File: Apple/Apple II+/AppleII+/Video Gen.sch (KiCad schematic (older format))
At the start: 46 parts, among them J14B Aux Video, K14 VIDEO OUT, Q3 2N3904, Q6 2N3904

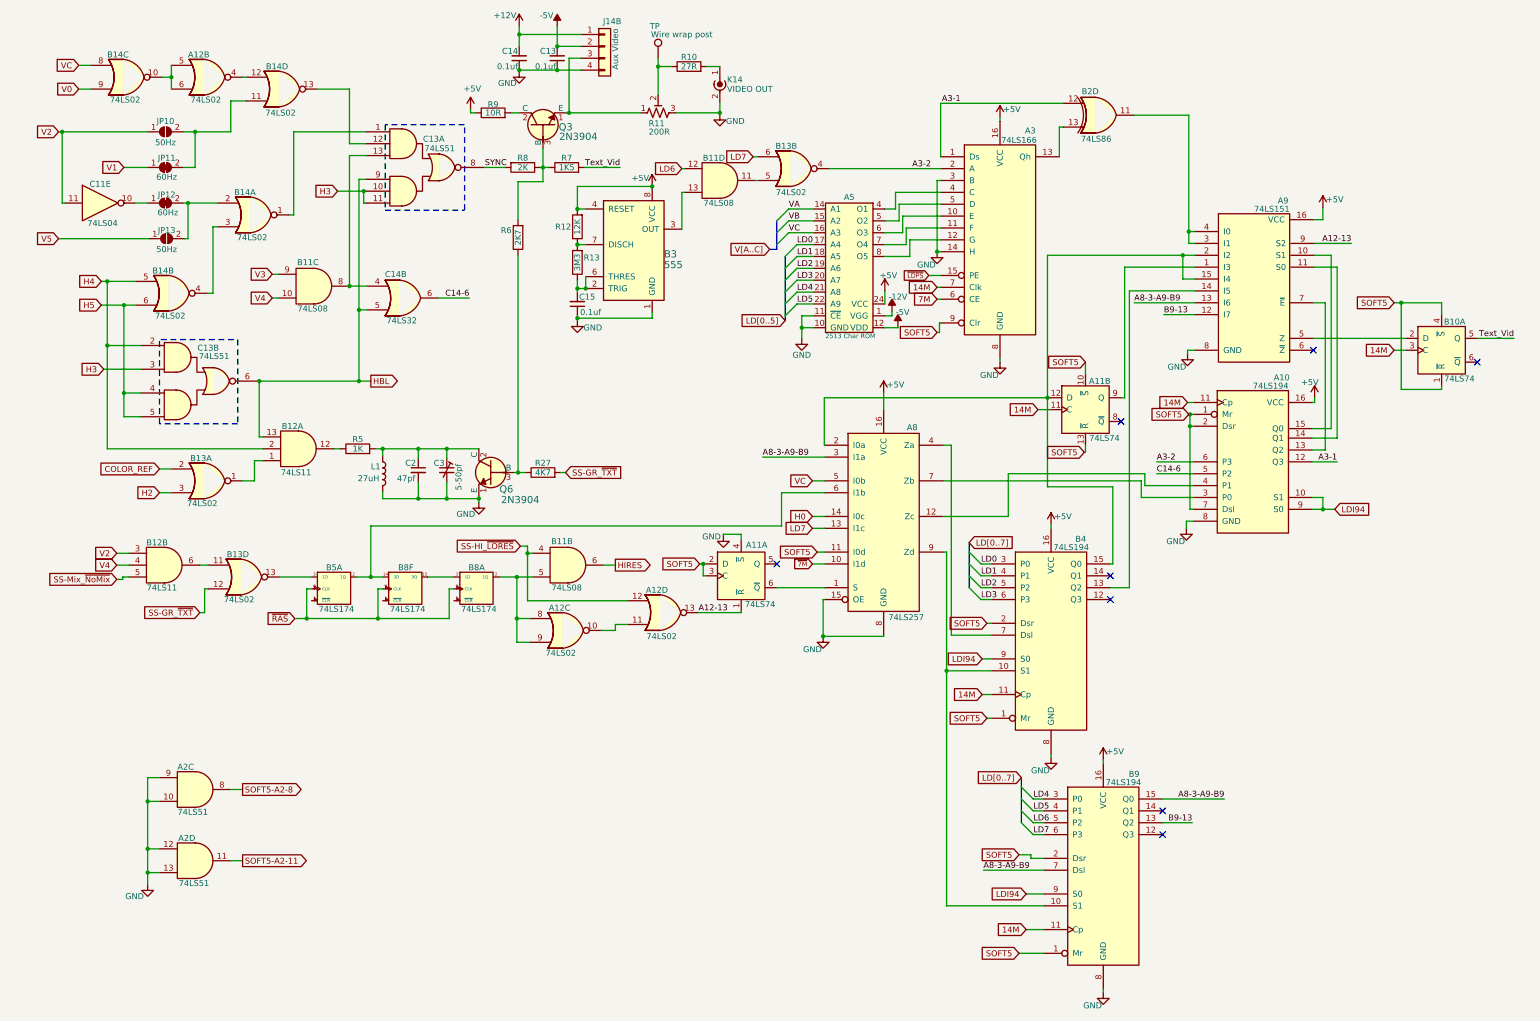
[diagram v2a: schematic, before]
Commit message: Created DiskII project folder and moved DiskII sheet to it, also fixed some signal designations, created sheet for peripheral slots
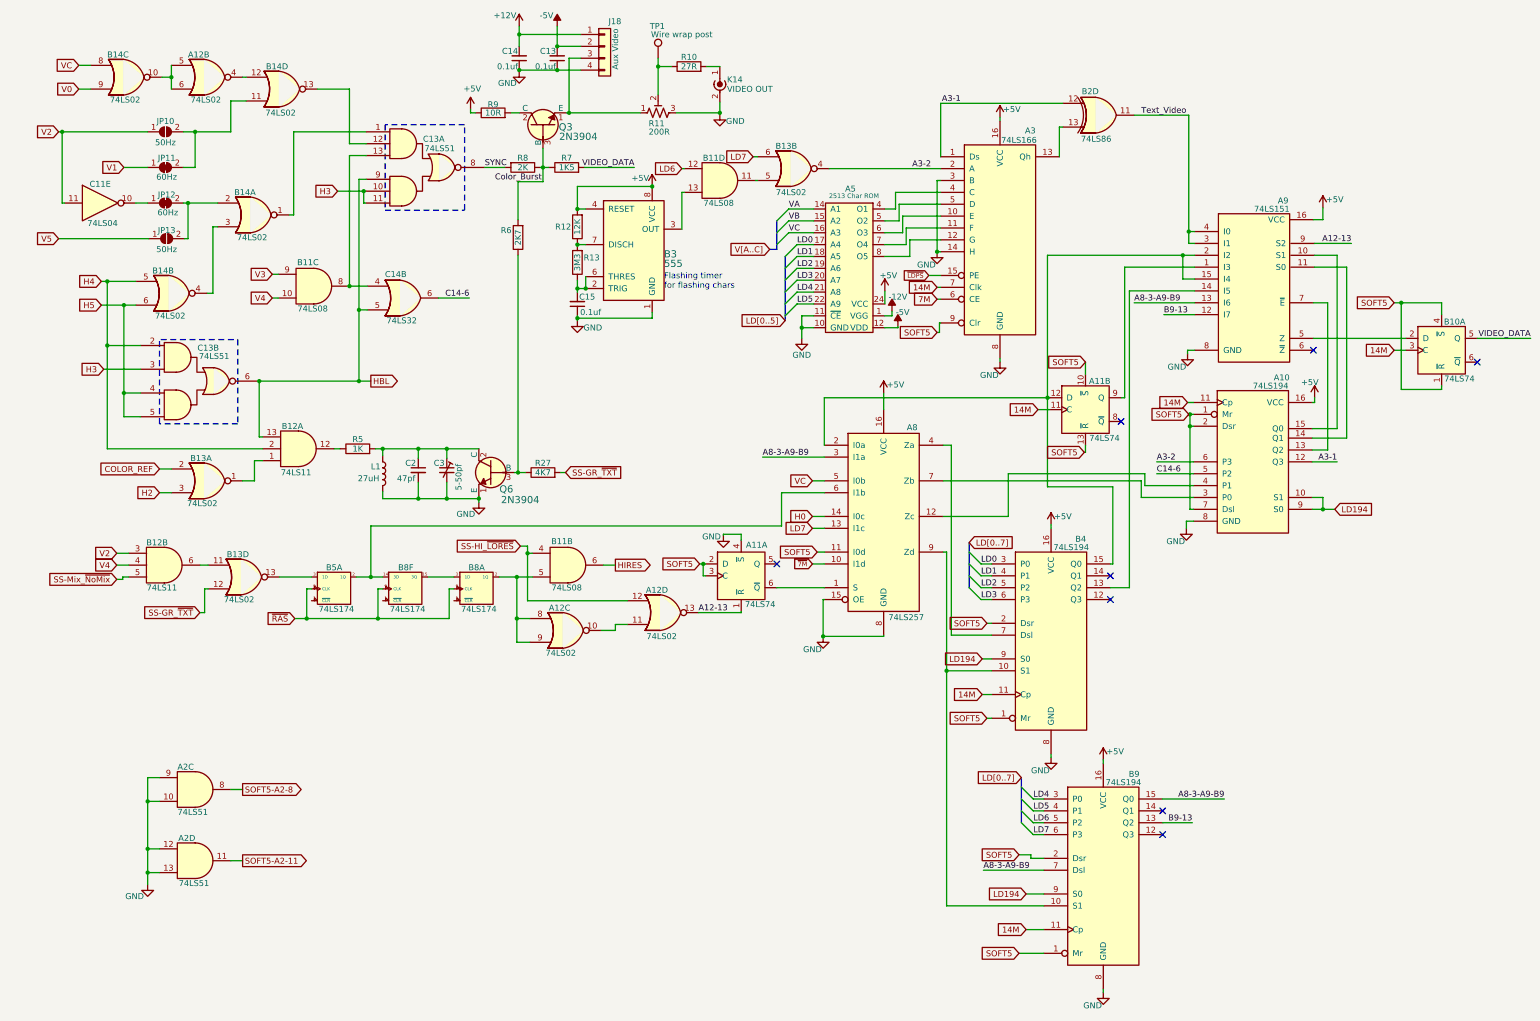
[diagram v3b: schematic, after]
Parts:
- renumbered J14B to J18, TP to TP1
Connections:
- net Text_Video: now reaches A9.3 (I1), A9.4 (I0), B2.11
- net Color_Burst: now reaches Q3.3 (B), R6.2, R7.1, R8.1
- net LDI94 renamed LD194
- net Text_Vid renamed VIDEO_DATA
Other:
- note added: "Flashing timer\nfor flashing chars"
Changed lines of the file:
@@
 $Descr A3 16535 11693
 encoding utf-8
-Sheet 9 9
+Sheet 8 9
 Title ""
 Date ""
@@
 $EndComp
 $Comp
-L power:+5V #PWR?
+L power:+5V #PWR0292
 U 1 1 633A8342
 P 4120 1370
-F 0 "#PWR?" H 4120 1220 50  0001 C CNN
+F 0 "#PWR0292" H 4120 1220 50  0001 C CNN
 F 1 "+5V" H 4135 1543 50  0000 C CNN
 F 2 "" H 4120 1370 50  0001 C CNN
@@
 	3920 4230 3680 4230
 $Comp
-L power:GND #PWR?
+L power:GND #PWR0293
 U 1 1 60A38A98
 P 4190 4680
-F 0 "#PWR?" H 4190 4430 50  0001 C CNN
+F 0 "#PWR0293" H 4190 4430 50  0001 C CNN
 F 1 "GND" H 4080 4580 50  0000 C CNN
 F 2 "" H 4190 4680 50  0001 C CNN
@@
 	6080 5200 6100 5200
 $Comp
-L power:GND #PWR?
+L power:GND #PWR0294
 U 1 1 60EB9BE8
 P 6250 4960
-F 0 "#PWR?" H 6250 4710 50  0001 C CNN
+F 0 "#PWR0294" H 6250 4710 50  0001 C CNN
 F 1 "GND" H 6150 4950 50  0000 C CNN
 F 2 "" H 6250 4960 50  0001 C CNN
@@
 	6220 1010 6110 1010
 $Comp
-L Connector:TestPoint TP
+L Connector:TestPoint TP1
 U 1 1 60EEFAED
 P 5700 940
-F 0 "TP" H 5630 1210 50  0000 L CNN
+F 0 "TP1" H 5630 1210 50  0000 L CNN
 F 1 "Wire wrap post" H 5640 1140 50  0000 L CNN
 F 2 "" H 5900 940 50  0001 C CNN
@@
 	5850 1400 6220 1400
 $Comp
-L Connector_Generic:Conn_01x04 J14B
+L Connector_Generic:Conn_01x04 J18
 U 1 1 60F13050
 P 5250 840
-F 0 "J14B" H 5390 1050 50  0000 R CNN
+F 0 "J18" H 5390 1050 50  0000 R CNN
 F 1 "Aux Video" V 5340 990 50  0000 R CNN
 F 2 "" H 5250 840 50  0001 C CNN
@@
 	5700 1010 5700 1250
 $Comp
-L power:GND #PWR?
+L power:GND #PWR0295
 U 1 1 60F2A5BB
 P 4530 1050
-F 0 "#PWR?" H 4530 800 50  0001 C CNN
+F 0 "#PWR0295" H 4530 800 50  0001 C CNN
 F 1 "GND" H 4430 950 50  0000 C CNN
 F 2 "" H 4530 1050 50  0001 C CNN
@@
 	6220 1410 6220 1400
 $Comp
-L power:GND #PWR?
+L power:GND #PWR0296
 U 1 1 60EFDC78
 P 6220 1410
-F 0 "#PWR?" H 6220 1160 50  0001 C CNN
+F 0 "#PWR0296" H 6220 1160 50  0001 C CNN
 F 1 "GND" H 6350 1350 50  0000 C CNN
 F 2 "" H 6220 1410 50  0001 C CNN
@@
 $EndComp
 $Comp
-L power:-5V #PWR?
+L power:-5V #PWR0297
 U 1 1 60F96EC2
 P 4850 670
-F 0 "#PWR?" H 4850 770 50  0001 C CNN
+F 0 "#PWR0297" H 4850 770 50  0001 C CNN
 F 1 "-5V" H 4760 760 50  0000 C CNN
 F 2 "" H 4850 670 50  0001 C CNN
@@
 $EndComp
 $Comp
-L power:+12V #PWR?
+L power:+12V #PWR0298
 U 1 1 60F982A7
 P 4530 670
-F 0 "#PWR?" H 4530 520 50  0001 C CNN
+F 0 "#PWR0298" H 4530 520 50  0001 C CNN
 F 1 "+12V" H 4410 760 50  0000 C CNN
 F 2 "" H 4530 670 50  0001 C CNN
@@
 	5900 1870 5920 1870
 $Comp
-L power:+5V #PWR?
+L power:+5V #PWR0299
 U 1 1 610E9F76
 P 5650 2020
-F 0 "#PWR?" H 5650 1870 50  0001 C CNN
+F 0 "#PWR0299" H 5650 1870 50  0001 C CNN
 F 1 "+5V" H 5550 2090 50  0000 C CNN
 F 2 "" H 5650 2020 50  0001 C CNN
@@
 $EndComp
 $Comp
-L power:GND #PWR?
+L power:GND #PWR0300
 U 1 1 610FD215
 P 5020 3150
-F 0 "#PWR?" H 5020 2900 50  0001 C CNN
+F 0 "#PWR0300" H 5020 2900 50  0001 C CNN
 F 1 "GND" H 5150 3090 50  0000 C CNN
 F 2 "" H 5020 3150 50  0001 C CNN
@@
 P 5450 2380
 F 0 "B3" H 5750 2170 60  0000 L CNN
-F 1 "555" H 5750 2080 60  0000 L CNN
+F 1 "555" H 5750 2090 60  0000 L CNN
 F 2 "digikey-footprints:DIP-8_W7.62mm" H 5650 2580 60  0001 L CNN
 F 3 "http://www.ti.com/general/docs/suppproductinfo.tsp?distId=10&gotoUrl=http%3A%2F%2Fwww.ti.com%2Flit%2Fgpn%2Fne555" H 5650 2680 60  0001 L CNN
@@
 	9080 1520 9080 1770
 $Comp
-L power:+5V #PWR?
+L power:+5V #PWR0301
 U 1 1 60372078
 P 8580 1440
-F 0 "#PWR?" H 8580 1290 50  0001 C CNN
+F 0 "#PWR0301" H 8580 1290 50  0001 C CNN
 F 1 "+5V" H 8680 1510 50  0000 C CNN
 F 2 "" H 8580 1440 50  0001 C CNN
@@
 U 1 1 60387CD9
 P 7310 2410
-F 0 "A5" H 7310 2710 50  0000 C CNN
-F 1 "2513 Char ROM" H 7320 1540 39  0000 C CNN
+F 0 "A5" H 7320 2780 50  0000 C CNN
+F 1 "2513 Char ROM" H 7350 2720 39  0000 C CNN
 F 2 "" H 7310 2410 50  0001 C CNN
 F 3 "" H 7310 2410 50  0001 C CNN
@@
 	7820 2470 8080 2470
 $Comp
-L power:GND #PWR?
+L power:GND #PWR0302
 U 1 1 60423DD7
 P 6910 3300
-F 0 "#PWR?" H 6910 3050 50  0001 C CNN
+F 0 "#PWR0302" H 6910 3050 50  0001 C CNN
 F 1 "GND" H 6910 3160 50  0000 C CNN
 F 2 "" H 6910 3300 50  0001 C CNN
@@
 Connection ~ 6910 3210
 $Comp
-L power:-5V #PWR?
+L power:-5V #PWR0303
 U 1 1 605FD77D
 P 7720 3200
-F 0 "#PWR?" H 7720 3300 50  0001 C CNN
+F 0 "#PWR0303" H 7720 3300 50  0001 C CNN
 F 1 "-5V" H 7760 3320 50  0000 C CNN
 F 2 "" H 7720 3200 50  0001 C CNN
@@
 	7720 3200 7720 3210
 $Comp
-L power:-12V #PWR?
+L power:-12V #PWR0304
 U 1 1 6060C3B3
 P 7670 3070
-F 0 "#PWR?" H 7670 3170 50  0001 C CNN
+F 0 "#PWR0304" H 7670 3170 50  0001 C CNN
 F 1 "-12V" H 7720 3190 50  0000 C CNN
 F 2 "" H 7670 3070 50  0001 C CNN
@@
 	7670 3110 7670 3070
 $Comp
-L power:+5V #PWR?
+L power:+5V #PWR0305
 U 1 1 60619A26
 P 7610 2900
-F 0 "#PWR?" H 7610 2750 50  0001 C CNN
+F 0 "#PWR0305" H 7610 2750 50  0001 C CNN
 F 1 "+5V" H 7640 3030 50  0000 C CNN
 F 2 "" H 7610 2900 50  0001 C CNN
@@
 	7610 2900 7610 3010
 $Comp
-L power:GND #PWR?
+L power:GND #PWR0306
 U 1 1 60626CAA
 P 8050 2570
-F 0 "#PWR?" H 8050 2320 50  0001 C CNN
+F 0 "#PWR0306" H 8050 2320 50  0001 C CNN
 F 1 "GND" H 7960 2460 50  0000 C CNN
 F 2 "" H 8050 2570 50  0001 C CNN
@@
 	8070 3170 8080 3170
 $Comp
-L power:GND #PWR?
+L power:GND #PWR0307
 U 1 1 606A2FE0
 P 8580 3500
-F 0 "#PWR?" H 8580 3250 50  0001 C CNN
+F 0 "#PWR0307" H 8580 3250 50  0001 C CNN
 F 1 "GND" H 8490 3390 50  0000 C CNN
 F 2 "" H 8580 3500 50  0001 C CNN
@@
 	11540 2500 11230 2500
 Wire Wire Line
-	11210 4140 11420 4140
-Wire Wire Line
-	11230 2700 11420 2700
-Wire Wire Line
-	11420 2700 11420 4140
-Wire Wire Line
-	11230 2600 11370 2600
-Wire Wire Line
-	11370 2600 11370 4060
-Wire Wire Line
-	11370 4060 11210 4060
-Wire Wire Line
-	11220 3000 11320 3000
-Wire Wire Line
-	11320 3000 11320 4240
-Wire Wire Line
-	11320 4240 11210 4240
+	11210 4140 11500 4140
+Wire Wire Line
+	11230 2700 11500 2700
+Wire Wire Line
+	11500 2700 11500 4140
+Wire Wire Line
+	11230 2600 11420 2600
+Wire Wire Line
+	11420 2600 11420 4060
+Wire Wire Line
+	11420 4060 11210 4060
+Wire Wire Line
+	11220 3000 11340 3000
+Wire Wire Line
+	11340 3000 11340 4240
+Wire Wire Line
+	11340 4240 11210 4240
 Text Label 8090 1320 0    50   ~ 0
 A3-1
@@
 	8100 5100 8130 5100
 $Comp
-L power:GND #PWR?
+L power:GND #PWR0308
 U 1 1 609A40CE
 P 7090 5810
-F 0 "#PWR?" H 7090 5560 50  0001 C CNN
+F 0 "#PWR0308" H 7090 5560 50  0001 C CNN
 F 1 "GND" H 7000 5700 50  0000 C CNN
 F 2 "" H 7090 5810 50  0001 C CNN
@@
 $EndComp
 $Comp
-L power:GND #PWR?
+L power:GND #PWR0309
 U 1 1 609B5C55
 P 9010 6830
-F 0 "#PWR?" H 9010 6580 50  0001 C CNN
+F 0 "#PWR0309" H 9010 6580 50  0001 C CNN
 F 1 "GND" H 8920 6720 50  0000 C CNN
 F 2 "" H 9010 6830 50  0001 C CNN
@@
 $EndComp
 $Comp
-L power:GND #PWR?
+L power:GND #PWR0310
 U 1 1 609C7E0F
 P 10150 4900
-F 0 "#PWR?" H 10150 4650 50  0001 C CNN
+F 0 "#PWR0310" H 10150 4650 50  0001 C CNN
 F 1 "GND" H 10060 4790 50  0000 C CNN
 F 2 "" H 10150 4900 50  0001 C CNN
@@
 	10150 4840 10210 4840
 $Comp
-L power:GND #PWR?
+L power:GND #PWR0311
 U 1 1 609DB4A7
 P 10160 3430
-F 0 "#PWR?" H 10160 3180 50  0001 C CNN
+F 0 "#PWR0311" H 10160 3180 50  0001 C CNN
 F 1 "GND" H 10070 3320 50  0000 C CNN
 F 2 "" H 10160 3430 50  0001 C CNN
@@
 	10160 3400 10220 3400
 $Comp
-L power:+5V #PWR?
+L power:+5V #PWR0312
 U 1 1 60A00EE1
 P 7600 3760
-F 0 "#PWR?" H 7600 3610 50  0001 C CNN
+F 0 "#PWR0312" H 7600 3610 50  0001 C CNN
 F 1 "+5V" H 7700 3830 50  0000 C CNN
 F 2 "" H 7600 3760 50  0001 C CNN
@@
 	7600 3760 7600 3900
 $Comp
-L power:+5V #PWR?
+L power:+5V #PWR0313
 U 1 1 60A13322
 P 9010 4870
-F 0 "#PWR?" H 9010 4720 50  0001 C CNN
+F 0 "#PWR0313" H 9010 4720 50  0001 C CNN
 F 1 "+5V" H 9110 4940 50  0000 C CNN
 F 2 "" H 9010 4870 50  0001 C CNN
@@
 	7000 5200 7100 5200
 $Comp
-L power:+5V #PWR?
+L power:+5V #PWR0314
 U 1 1 60CEE1DD
 P 11300 2200
-F 0 "#PWR?" H 11300 2050 50  0001 C CNN
+F 0 "#PWR0314" H 11300 2050 50  0001 C CNN
 F 1 "+5V" H 11400 2270 50  0000 C CNN
 F 2 "" H 11300 2200 50  0001 C CNN
@@
 Wire Wire Line
 	11960 3000 12300 3000
-Text Label 12910 3300 2    50   ~ 0
-Text_Vid
-Wire Wire Line
-	12910 3300 12600 3300
-Text Label 5380 1860 2    50   ~ 0
-Text_Vid
-Wire Wire Line
-	5080 1860 5380 1860
+Text Label 13050 3300 2    50   ~ 0
+VIDEO_DATA
+Wire Wire Line
+	13050 3300 12600 3300
+Wire Wire Line
+	5080 1860 5500 1860
 Connection ~ 5650 2020
 Wire Wire Line
@@
 Connection ~ 10180 4040
 $Comp
-L power:+5V #PWR?
+L power:+5V #PWR0315
 U 1 1 60FA1798
 P 11230 3800
-F 0 "#PWR?" H 11230 3650 50  0001 C CNN
+F 0 "#PWR0315" H 11230 3650 50  0001 C CNN
 F 1 "+5V" H 11190 3930 50  0000 C CNN
 F 2 "" H 11230 3800 50  0001 C CNN
@@
 	11230 3840 11210 3840
 Text GLabel 11400 4740 2    50   Input ~ 0
-LDI94
+LD194
 Wire Wire Line
 	11400 4740 11300 4740
@@
 	11300 4740 11210 4740
 Text GLabel 8430 6000 0    50   Input ~ 0
-LDI94
+LD194
 Wire Wire Line
 	8430 6000 8510 6000
 Text GLabel 8800 7980 0    50   Input ~ 0
-LDI94
+LD194
 Wire Wire Line
 	8800 7980 8950 7980
@@
 LD[0..7]
 $Comp
-L power:+5V #PWR?
+L power:+5V #PWR0316
 U 1 1 6131FA02
 P 9450 6850
-F 0 "#PWR?" H 9450 6700 50  0001 C CNN
+F 0 "#PWR0316" H 9450 6700 50  0001 C CNN
 F 1 "+5V" H 9550 6920 50  0000 C CNN
 F 2 "" H 9450 6850 50  0001 C CNN
@@
 $EndComp
 $Comp
-L power:GND #PWR?
+L power:GND #PWR0317
 U 1 1 61320357
 P 9450 8810
-F 0 "#PWR?" H 9450 8560 50  0001 C CNN
+F 0 "#PWR0317" H 9450 8560 50  0001 C CNN
 F 1 "GND" H 9360 8700 50  0000 C CNN
 F 2 "" H 9450 8810 50  0001 C CNN
@@
 $EndComp
 $Comp
-L power:GND #PWR?
+L power:GND #PWR0318
 U 1 1 6147ADD1
 P 1400 7900
-F 0 "#PWR?" H 1400 7650 50  0001 C CNN
+F 0 "#PWR0318" H 1400 7650 50  0001 C CNN
 F 1 "GND" H 1290 7800 50  0000 C CNN
 F 2 "" H 1400 7900 50  0001 C CNN
@@
 Wire Wire Line
 	2200 7700 2100 7700
+Text Label 5500 1860 2    50   ~ 0
+VIDEO_DATA
+Text Label 4720 1980 2    50   ~ 0
+Color_Burst
+Text Label 9770 1420 0    50   ~ 0
+Text_Video
+Text Notes 5750 2890 0    50   ~ 0
+Flashing timer\nfor flashing chars
 Wire Bus Line
 	6700 2310 6700 2550
